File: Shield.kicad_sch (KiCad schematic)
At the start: 9 parts, among them U1 MIC5219-3.3YM5, U2 MIC5219-3.3YM5

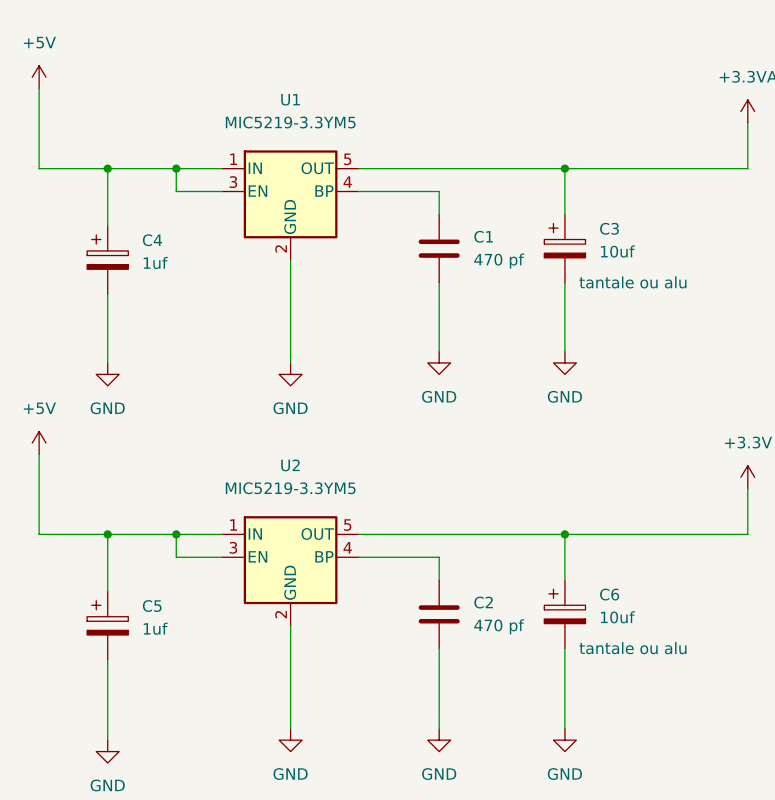
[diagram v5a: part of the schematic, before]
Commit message: Change le regulateur, le microchip est dur a avoir
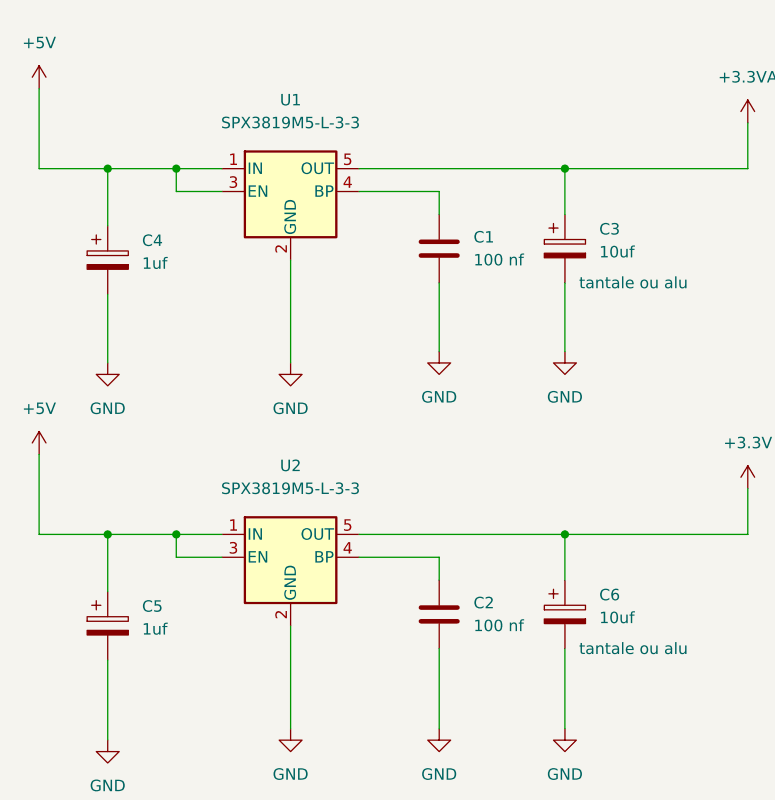
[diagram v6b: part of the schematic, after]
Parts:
- removed U1, U2: MIC5219-3.3YM5, Package_TO_SOT_SMD:SOT-23-5, symbol Regulator_Linear:MIC5219-3.3YM5
- added U1, U2: SPX3819M5-L-3-3, Package_TO_SOT_SMD:SOT-23-5, symbol Regulator_Linear:SPX3819M5-L-3-3
- C1, C2: value 470 pf -> 100 nf
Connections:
- net +3.3V: now also U2.5 (OUT)
- net +3.3VA: now also U1.5 (OUT)
- net +5V: now also U1.1 (IN), U1.3 (EN), U2.1 (IN), U2.3 (EN)
- net GND: now also U1.2 (GND), U2.2 (GND)
- net at C2.1: now also U2.4 (BP)
- net at C1.1: now also U1.4 (BP)
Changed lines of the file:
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@@
     (pin "1")
   )
-  (symbol (lib_id "power:+5V") (at 170.18 33.02 0) (unit 1)
-    (in_bom yes) (on_board yes) (fields_autoplaced)
-    (property "Reference" "#PWR015" (id 0) (at 170.18 36.83 0)
-      (effects (font (size 1.27 1.27)) hide)
-    )
-    (property "Value" "+5V" (id 1) (at 170.18 27.94 0))
-    (property "Footprint" "" (id 2) (at 170.18 33.02 0)
-      (effects (font (size 1.27 1.27)) hide)
-    )
-    (property "Datasheet" "" (id 3) (at 170.18 33.02 0)
-      (effects (font (size 1.27 1.27)) hide)
-    )
-    (pin "1")
-  )
-  (symbol (lib_id "Device:C") (at 68.58 81.28 0) (unit 1)
-    (in_bom yes) (on_board yes) (fields_autoplaced)
-    (property "Reference" "C2" (id 0) (at 72.39 80.0099 0)
-      (effects (font (size 1.27 1.27)) (justify left))
-    )
-    (property "Value" "470 pf" (id 1) (at 72.39 82.5499 0)
-      (effects (font (size 1.27 1.27)) (justify left))
-    )
-    (property "Footprint" "Capacitor_SMD:C_0603_1608Metric_Pad1.08x0.95mm_HandSolder" (id 2) (at 69.5452 85.09 0)
-      (effects (font (size 1.27 1.27)) hide)
-    )
-    (property "Datasheet" "~" (id 3) (at 68.58 81.28 0)
-      (effects (font (size 1.27 1.27)) hide)
-    )
-    (pin "1")
-    (pin "2")
-  )
-  (symbol (lib_id "power:+3.3VA") (at 102.87 26.67 0) (unit 1)
-    (in_bom yes) (on_board yes) (fields_autoplaced)
-    (property "Reference" "#PWR09" (id 0) (at 102.87 30.48 0)
-      (effects (font (size 1.27 1.27)) hide)
-    )
-    (property "Value" "+3.3VA" (id 1) (at 102.87 21.59 0))
-    (property "Footprint" "" (id 2) (at 102.87 26.67 0)
-      (effects (font (size 1.27 1.27)) hide)
-    )
-    (property "Datasheet" "" (id 3) (at 102.87 26.67 0)
-      (effects (font (size 1.27 1.27)) hide)
-    )
-    (pin "1")
-  )
-  (symbol (lib_id "Regulator_Linear:MIC5219-3.3YM5") (at 52.07 74.93 0) (unit 1)
-    (in_bom yes) (on_board yes) (fields_autoplaced)
-    (property "Reference" "U2" (id 0) (at 52.07 64.77 0))
-    (property "Value" "MIC5219-3.3YM5" (id 1) (at 52.07 67.31 0))
-    (property "Footprint" "Package_TO_SOT_SMD:SOT-23-5" (id 2) (at 52.07 66.675 0)
-      (effects (font (size 1.27 1.27)) hide)
-    )
-    (property "Datasheet" "http://ww1.microchip.com/downloads/en/DeviceDoc/MIC5219-500mA-Peak-Output-LDO-Regulator-DS20006021A.pdf" (id 3) (at 52.07 74.93 0)
+  (symbol (lib_id "Regulator_Linear:SPX3819M5-L-3-3") (at 52.07 34.29 0) (unit 1)
+    (in_bom yes) (on_board yes) (fields_autoplaced)
+    (property "Reference" "U1" (id 0) (at 52.07 24.13 0))
+    (property "Value" "SPX3819M5-L-3-3" (id 1) (at 52.07 26.67 0))
+    (property "Footprint" "Package_TO_SOT_SMD:SOT-23-5" (id 2) (at 52.07 26.035 0)
+      (effects (font (size 1.27 1.27)) hide)
+    )
+    (property "Datasheet" "https://www.exar.com/content/document.ashx?id=22106&languageid=1033&type=Datasheet&partnumber=SPX3819&filename=SPX3819.pdf&part=SPX3819" (id 3) (at 52.07 34.29 0)
       (effects (font (size 1.27 1.27)) hide)
     )
@@
     (pin "5")
   )
+  (symbol (lib_id "power:+5V") (at 170.18 33.02 0) (unit 1)
+    (in_bom yes) (on_board yes) (fields_autoplaced)
+    (property "Reference" "#PWR015" (id 0) (at 170.18 36.83 0)
+      (effects (font (size 1.27 1.27)) hide)
+    )
+    (property "Value" "+5V" (id 1) (at 170.18 27.94 0))
+    (property "Footprint" "" (id 2) (at 170.18 33.02 0)
+      (effects (font (size 1.27 1.27)) hide)
+    )
+    (property "Datasheet" "" (id 3) (at 170.18 33.02 0)
+      (effects (font (size 1.27 1.27)) hide)
+    )
+    (pin "1")
+  )
+  (symbol (lib_id "Device:C") (at 68.58 81.28 0) (unit 1)
+    (in_bom yes) (on_board yes) (fields_autoplaced)
+    (property "Reference" "C2" (id 0) (at 72.39 80.0099 0)
+      (effects (font (size 1.27 1.27)) (justify left))
+    )
+    (property "Value" "100 nf" (id 1) (at 72.39 82.5499 0)
+      (effects (font (size 1.27 1.27)) (justify left))
+    )
+    (property "Footprint" "Capacitor_SMD:C_0603_1608Metric_Pad1.08x0.95mm_HandSolder" (id 2) (at 69.5452 85.09 0)
+      (effects (font (size 1.27 1.27)) hide)
+    )
+    (property "Datasheet" "~" (id 3) (at 68.58 81.28 0)
+      (effects (font (size 1.27 1.27)) hide)
+    )
+    (pin "1")
+    (pin "2")
+  )
+  (symbol (lib_id "Regulator_Linear:SPX3819M5-L-3-3") (at 52.07 74.93 0) (unit 1)
+    (in_bom yes) (on_board yes) (fields_autoplaced)
+    (property "Reference" "U2" (id 0) (at 52.07 64.77 0))
+    (property "Value" "SPX3819M5-L-3-3" (id 1) (at 52.07 67.31 0))
+    (property "Footprint" "Package_TO_SOT_SMD:SOT-23-5" (id 2) (at 52.07 66.675 0)
+      (effects (font (size 1.27 1.27)) hide)
+    )
+    (property "Datasheet" "https://www.exar.com/content/document.ashx?id=22106&languageid=1033&type=Datasheet&partnumber=SPX3819&filename=SPX3819.pdf&part=SPX3819" (id 3) (at 52.07 74.93 0)
+      (effects (font (size 1.27 1.27)) hide)
+    )
+    (pin "1")
+    (pin "2")
+    (pin "3")
+    (pin "4")
+    (pin "5")
+  )
+  (symbol (lib_id "power:+3.3VA") (at 102.87 26.67 0) (unit 1)
+    (in_bom yes) (on_board yes) (fields_autoplaced)
+    (property "Reference" "#PWR09" (id 0) (at 102.87 30.48 0)
+      (effects (font (size 1.27 1.27)) hide)
+    )
+    (property "Value" "+3.3VA" (id 1) (at 102.87 21.59 0))
+    (property "Footprint" "" (id 2) (at 102.87 26.67 0)
+      (effects (font (size 1.27 1.27)) hide)
+    )
+    (property "Datasheet" "" (id 3) (at 102.87 26.67 0)
+      (effects (font (size 1.27 1.27)) hide)
+    )
+    (pin "1")
+  )
   (symbol (lib_id "power:GND") (at 52.07 53.34 0) (unit 1)
     (in_bom yes) (on_board yes) (fields_autoplaced)
@@
       (effects (font (size 1.27 1.27)) (justify left))
     )
-    (property "Value" "470 pf" (id 1) (at 72.39 41.9099 0)
+    (property "Value" "100 nf" (id 1) (at 72.39 41.9099 0)
       (effects (font (size 1.27 1.27)) (justify left))
     )
@@
     (pin "1")
     (pin "2")
-  )
-  (symbol (lib_id "Regulator_Linear:MIC5219-3.3YM5") (at 52.07 34.29 0) (unit 1)
-    (in_bom yes) (on_board yes) (fields_autoplaced)
-    (property "Reference" "U1" (id 0) (at 52.07 24.13 0))
-    (property "Value" "MIC5219-3.3YM5" (id 1) (at 52.07 26.67 0))
-    (property "Footprint" "Package_TO_SOT_SMD:SOT-23-5" (id 2) (at 52.07 26.035 0)
-      (effects (font (size 1.27 1.27)) hide)
-    )
-    (property "Datasheet" "http://ww1.microchip.com/downloads/en/DeviceDoc/MIC5219-500mA-Peak-Output-LDO-Regulator-DS20006021A.pdf" (id 3) (at 52.07 34.29 0)
-      (effects (font (size 1.27 1.27)) hide)
-    )
-    (pin "1")
-    (pin "2")
-    (pin "3")
-    (pin "4")
-    (pin "5")
   )
   (symbol (lib_id "MCU_Module:Arduino_UNO_R3") (at 165.1 62.23 0) (unit 1)
@@
     )
     (path "/c49d794b-82e9-493d-b715-0ad5480931c3"
-      (reference "C1") (unit 1) (value "470 pf") (footprint "Capacitor_SMD:C_0603_1608Metric_Pad1.08x0.95mm_HandSolder")
+      (reference "C1") (unit 1) (value "100 nf") (footprint "Capacitor_SMD:C_0603_1608Metric_Pad1.08x0.95mm_HandSolder")
     )
     (path "/86a05c3c-54d2-4977-bcb6-ee4c0872ef57"
-      (reference "C2") (unit 1) (value "470 pf") (footprint "Capacitor_SMD:C_0603_1608Metric_Pad1.08x0.95mm_HandSolder")
+      (reference "C2") (unit 1) (value "100 nf") (footprint "Capacitor_SMD:C_0603_1608Metric_Pad1.08x0.95mm_HandSolder")
     )
     (path "/b0f180b9-4197-4edd-b5e1-238f1d62e083"
@@
       (reference "R4") (unit 1) (value "400 0.1%") (footprint "Resistor_SMD:R_1206_3216Metric_Pad1.30x1.75mm_HandSolder")
     )
-    (path "/dd1c16a7-671a-4e62-b647-9fcd8906b509"
-      (reference "U1") (unit 1) (value "MIC5219-3.3YM5") (footprint "Package_TO_SOT_SMD:SOT-23-5")
-    )
-    (path "/96e203a9-b5da-4ee0-8051-ae09c0cbe467"
-      (reference "U2") (unit 1) (value "MIC5219-3.3YM5") (footprint "Package_TO_SOT_SMD:SOT-23-5")
+    (path "/70166011-cdbf-484f-91f0-717371ba961c"
+      (reference "U1") (unit 1) (value "SPX3819M5-L-3-3") (footprint "Package_TO_SOT_SMD:SOT-23-5")
+    )
+    (path "/86be4467-fe1b-4535-b56f-318f0aa66c4b"
+      (reference "U2") (unit 1) (value "SPX3819M5-L-3-3") (footprint "Package_TO_SOT_SMD:SOT-23-5")
     )
     (path "/ec1f69e3-5897-4f77-9f27-39305d91428f/0f7ebff1-b6a9-4a4c-9024-61e0cb0cec58"

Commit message: v002
AJoute des grains de café pour choisir le chip select
Miroir connecteur arduiono
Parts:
- added JP1, JP2, JP3, JP4, JP5, JP6, JP7, JP8: SolderJumper_2_Open, Jumper:SolderJumper-2_P1.3mm_Open_RoundedPad1.0x1.5mm, symbol Jumper:SolderJumper_2_Open
- added JP10, JP11, JP12, JP9: SolderJumper_2_Bridged, Jumper:SolderJumper-2_P1.3mm_Open_RoundedPad1.0x1.5mm, symbol Jumper:SolderJumper_2_Bridged
- C1, C2: value 100 nf -> 100 nF
- C3, C6: value 10uf -> 10uF
- C4, C5: value 1uf -> 1uF
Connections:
- net CS_MAX1: now also JP1.1 (A), JP5.1 (A), JP9.2 (B); no longer A1.9 (A0)
- net CS_MAX2: now also JP10.2 (B), JP2.1 (A), JP6.1 (A); no longer A1.10 (A1)
- net CS_MAX3: now also JP11.2 (B), JP3.1 (A), JP7.1 (A); no longer A1.11 (A2)
- net CS_MAX4: now also JP12.2 (B), JP4.1 (A), JP8.1 (A); no longer A1.12 (A3)
- net at A1.17 (D2): now also JP1.2 (B)
- net at A1.18 (D3): now also JP2.2 (B)
- net at A1.19 (D4): now also JP3.2 (B)
- net at A1.20 (D5): now also JP4.2 (B)
- net at A1.21 (D6): now also JP5.2 (B)
- net at A1.22 (D7): now also JP6.2 (B)
- net at A1.23 (D8): now also JP7.2 (B)
- net at A1.24 (D9): now also JP8.2 (B)
- new net: A1.11 (A2), JP11.1 (A)
- new net: A1.9 (A0), JP9.1 (A)
- new net: A1.10 (A1), JP10.1 (A)
- new net: A1.12 (A3), JP12.1 (A)
- no-connect marks 20 -> 12

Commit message: Ajoute img et update connecteur avec 3d
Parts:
- A1: footprint Module:Arduino_UNO_R3 -> Arduino:Arduino_UNO_R3_3d
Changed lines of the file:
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@@
       (effects (font (size 1.27 1.27)) (justify left))
     )
-    (property "Footprint" "Module:Arduino_UNO_R3" (id 2) (at 165.1 62.23 0)
+    (property "Footprint" "Arduino:Arduino_UNO_R3_3d" (id 2) (at 165.1 62.23 0)
       (effects (font (size 1.27 1.27) italic) hide)
     )
@@
     )
     (path "/e6a0dfad-b3ab-4c36-83bb-45ac5b045ec9"
-      (reference "A1") (unit 1) (value "Arduino_UNO_R3") (footprint "Module:Arduino_UNO_R3")
+      (reference "A1") (unit 1) (value "Arduino_UNO_R3") (footprint "Arduino:Arduino_UNO_R3_3d")
     )
     (path "/c49d794b-82e9-493d-b715-0ad5480931c3"
